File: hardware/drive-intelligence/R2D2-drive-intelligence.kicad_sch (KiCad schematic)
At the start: 36 parts, among them J1 Conn_01x05_Pin, J2 1751248, J3 1751248, J4 1751248, J5 1725669, SW1 PTS636 SM50J SMTR LFS, U1 STM32F042F6Px, U2 SN65HVD230, U3 LM1117MP-3.3, U4 LMV321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

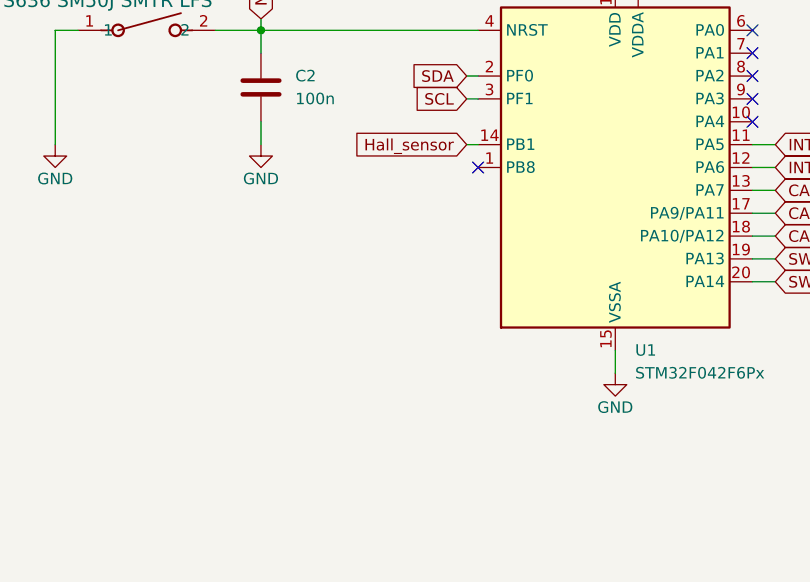
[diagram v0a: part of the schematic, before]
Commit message: hw: drive-intelligence: added solder jumper for left or right motor setting
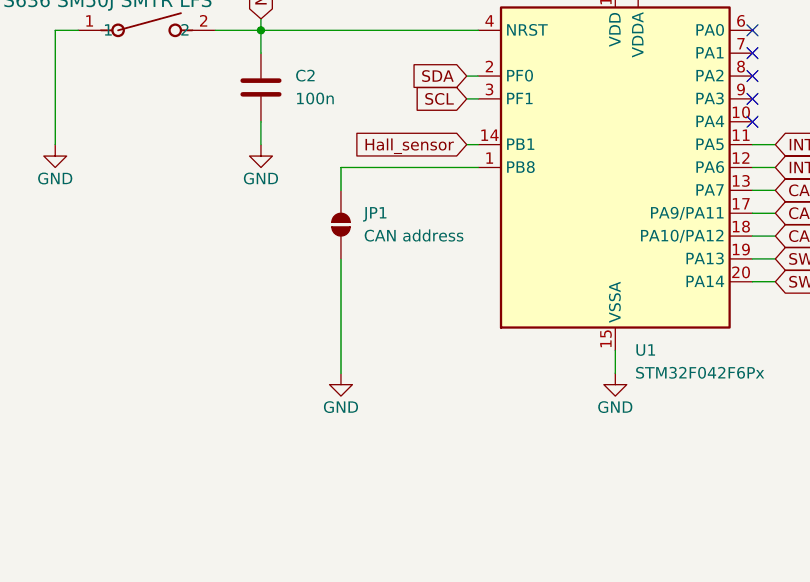
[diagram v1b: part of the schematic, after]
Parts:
- added JP1: CAN address, Jumper:SolderJumper-2_P1.3mm_Open_TrianglePad1.0x1.5mm, symbol Jumper:SolderJumper_2_Open
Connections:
- net GND: now also JP1.1 (A)
- net at U1.1 (PB8): now also JP1.2 (B)
- no-connect marks 9 -> 8
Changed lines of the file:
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@@
 (kicad_sch
-	(version 20231120)
+	(version 20250114)
 	(generator "eeschema")
-	(generator_version "8.0")
+	(generator_version "9.0")
 	(paper "A4")
 	(title_block
@@
 	)
 	(no_connect
-		(at 220.98 49.53)
+		(at 220.98 57.15)
 	)
 	(no_connect
-		(at 190.5 62.23)
+		(at 220.98 49.53)
 	)
 	(no_connect
@@
 	)
 	(no_connect
-		(at 220.98 57.15)
-	)
-	(no_connect
 		(at 58.42 96.52)
 	)
@@
 	(wire
 		(pts
+			(xy 175.26 62.23) (xy 190.5 62.23)
+		)
+		(stroke
+			(width 0)
+			(type default)
+		)
+	)
+	(wire
+		(pts
 			(xy 200.66 143.51) (xy 200.66 140.97)
 		)
@@
 	(wire
 		(pts
+			(xy 175.26 64.77) (xy 175.26 62.23)
+		)
+		(stroke
+			(width 0)
+			(type default)
+		)
+	)
+	(wire
+		(pts
 			(xy 254 124.46) (xy 254 123.19)
 		)
@@
 	(wire
 		(pts
+			(xy 175.26 72.39) (xy 175.26 85.09)
+		)
+		(stroke
+			(width 0)
+			(type default)
+		)
+	)
+	(wire
+		(pts
 			(xy 36.83 49.53) (xy 40.64 49.53)
 		)
@@
 	)
 	(symbol
+		(lib_id "Jumper:SolderJumper_2_Open")
+		(at 175.26 68.58 90)
+		(unit 1)
+		(exclude_from_sim yes)
+		(in_bom no)
+		(on_board yes)
+		(dnp no)
+		(fields_autoplaced yes)
+		(property "Reference" "JP1"
+			(at 177.8 67.3099 90)
+			(effects
+				(font
+					(size 1.27 1.27)
+				)
+				(justify right)
+			)
+		)
+		(property "Value" "CAN address"
+			(at 177.8 69.8499 90)
+			(effects
+				(font
+					(size 1.27 1.27)
+				)
+				(justify right)
+			)
+		)
+		(property "Footprint" "Jumper:SolderJumper-2_P1.3mm_Open_TrianglePad1.0x1.5mm"
+			(at 175.26 68.58 0)
+			(effects
+				(font
+					(size 1.27 1.27)
+				)
+				(hide yes)
+			)
+		)
+		(property "Datasheet" "~"
+			(at 175.26 68.58 0)
+			(effects
+				(font
+					(size 1.27 1.27)
+				)
+				(hide yes)
+			)
+		)
+		(property "Description" "Solder Jumper, 2-pole, open"
+			(at 175.26 68.58 0)
+			(effects
+				(font
+					(size 1.27 1.27)
+				)
+				(hide yes)
+			)
+		)
+		(pin "1"
+		)
+		(pin "2"
+		)
+		(instances
+			(project ""
+				(path "/7f4fad22-6ce0-40fd-8101-aa8e03cbc6ce"
+					(reference "JP1")
+					(unit 1)
+				)
+			)
+		)
+	)
+	(symbol
 		(lib_id "power:GND")
 		(at 254 124.46 0)
@@
 	)
 	(symbol
+		(lib_id "power:GND")
+		(at 175.26 85.09 0)
+		(unit 1)
+		(exclude_from_sim no)
+		(in_bom yes)
+		(on_board yes)
+		(dnp no)
+		(property "Reference" "#PWR040"
+			(at 175.26 91.44 0)
+			(effects
+				(font
+					(size 1.27 1.27)
+				)
+				(hide yes)
+			)
+		)
+		(property "Value" "GND"
+			(at 175.26 88.9 0)
+			(effects
+				(font
+					(size 1.27 1.27)
+				)
+			)
+		)
+		(property "Footprint" ""
+			(at 175.26 85.09 0)
+			(effects
+				(font
+					(size 1.27 1.27)
+				)
+				(hide yes)
+			)
+		)
+		(property "Datasheet" ""
+			(at 175.26 85.09 0)
+			(effects
+				(font
+					(size 1.27 1.27)
+				)
+				(hide yes)
+			)
+		)
+		(property "Description" "Power symbol creates a global label with name \"GND\" , ground"
+			(at 175.26 85.09 0)
+			(effects
+				(font
+					(size 1.27 1.27)
+				)
+				(hide yes)
+			)
+		)
+		(pin "1"
+		)
+		(instances
+			(project "R2D2-drive-intelligence"
+				(path "/7f4fad22-6ce0-40fd-8101-aa8e03cbc6ce"
+					(reference "#PWR040")
+					(unit 1)
+				)
+			)
+		)
+	)
+	(symbol
 		(lib_id "Device:C")
 		(at 90.17 30.48 0)
@@
 		)
 	)
+	(embedded_fonts no)
 )
